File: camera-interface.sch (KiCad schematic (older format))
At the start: 30 parts, among them J8 WE_68715014522, U19 NTS0102GT, U20 NTS0102GT, U22 AP2114H-3_3TRG1

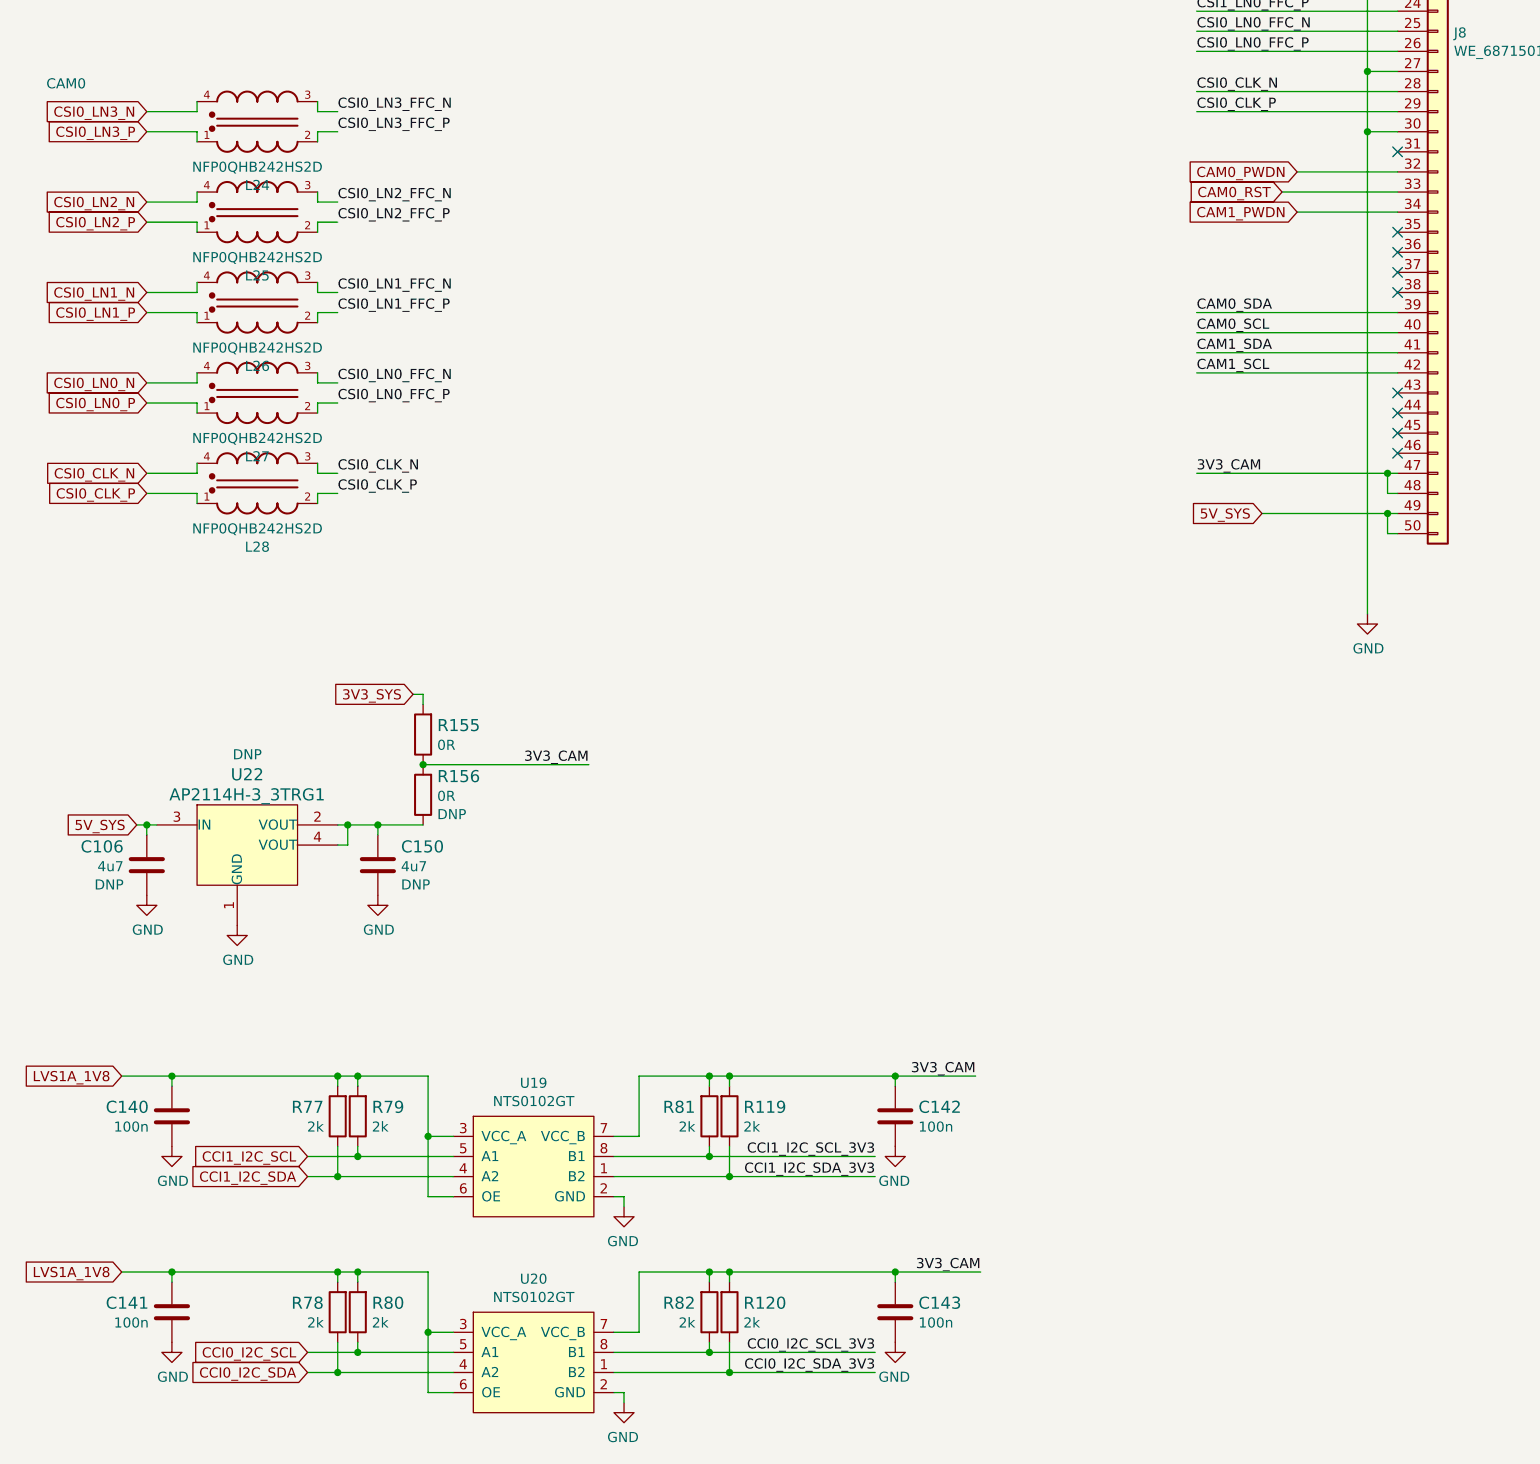
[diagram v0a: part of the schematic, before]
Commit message: Add test points
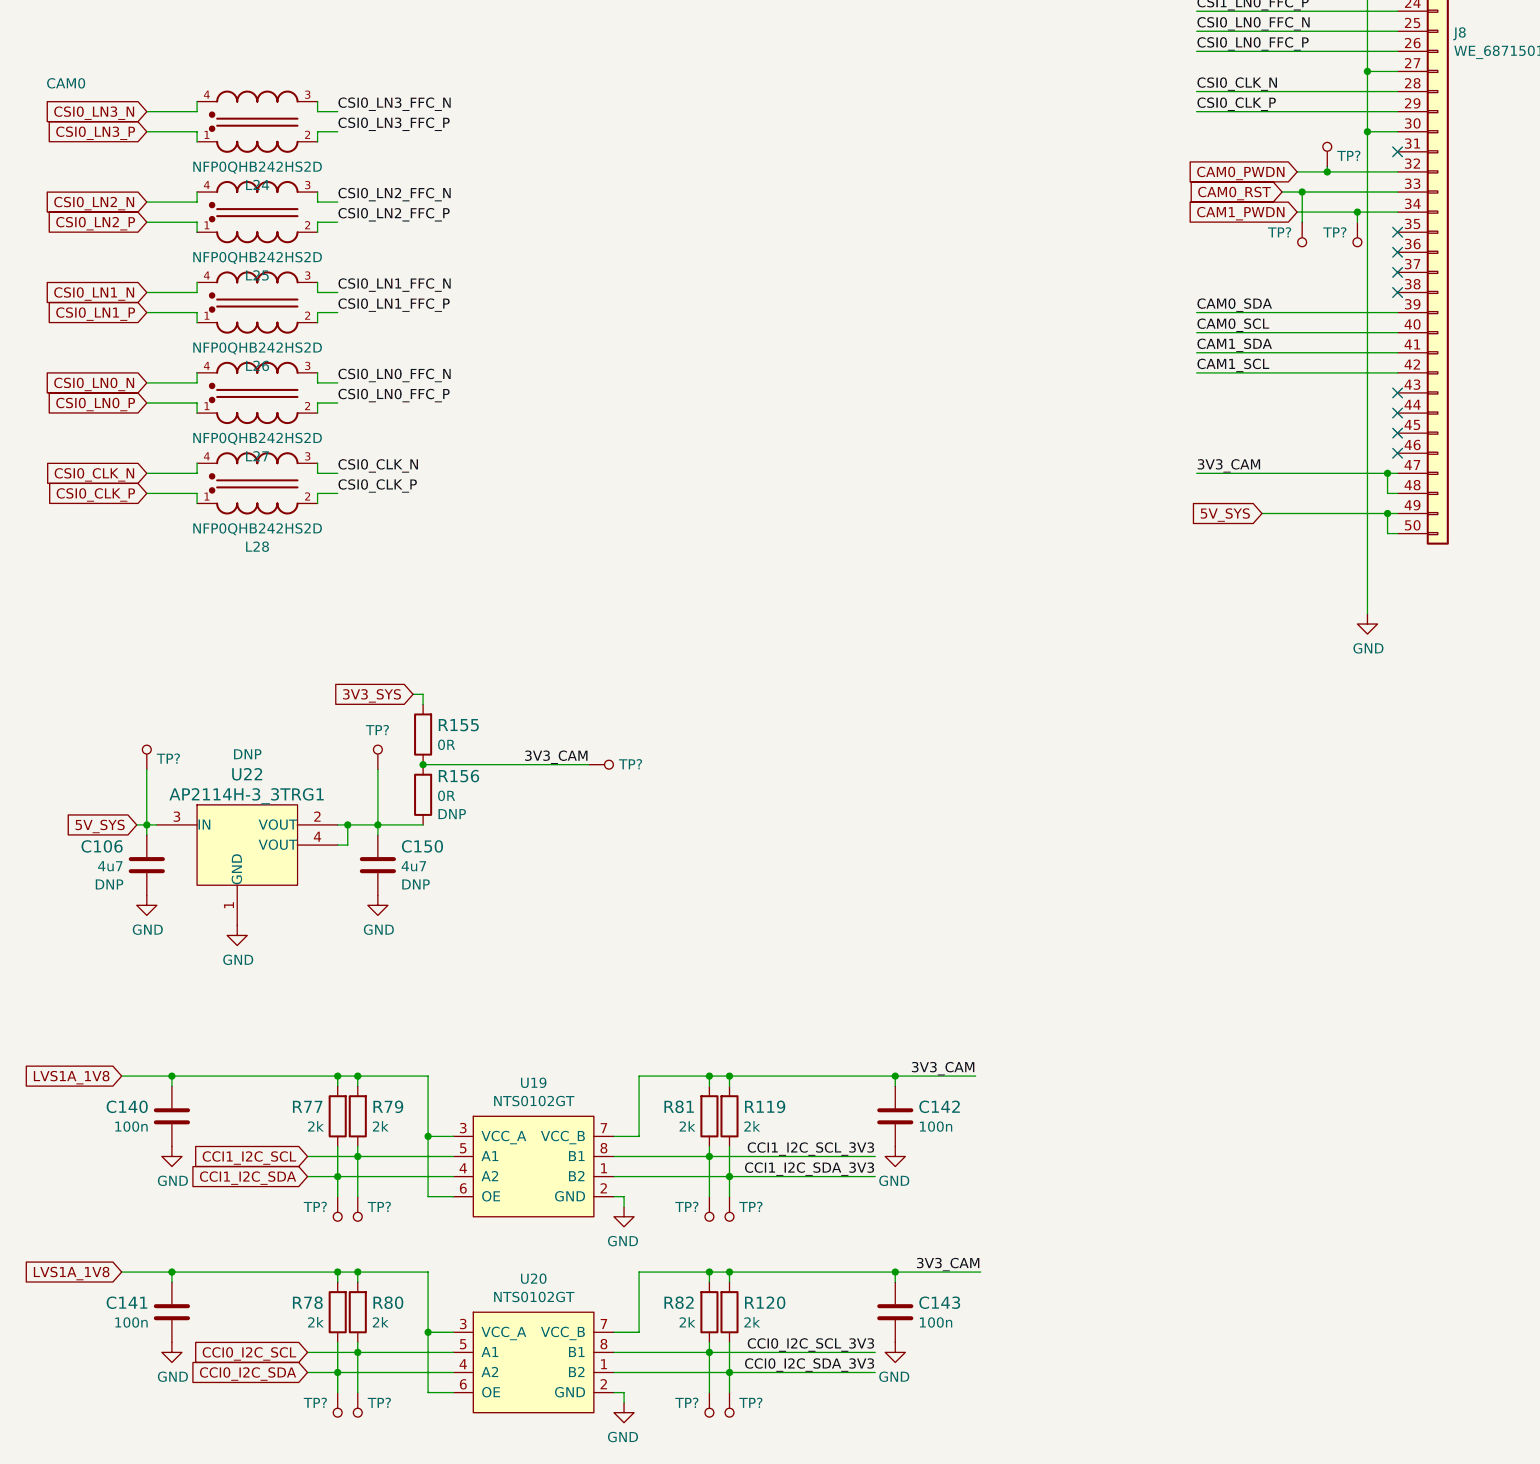
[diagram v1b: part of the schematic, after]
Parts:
- added TP? (x14): TP_SMD_0_75MM, antmicro-footprints:Testpoint_smd_0_75mm, symbol antmicroTestPoints:TP_SMD_0_75MM
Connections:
- net 3V3_CAM: now also TP?.1
- net 5V_SYS: now also TP?.1
- net CAM0_PWDN: now also TP?.1
- net CAM0_RST: now also TP?.1
- net CAM1_PWDN: now also TP?.1
- net CCI0_I2C_SCL: now also TP?.1
- net CCI0_I2C_SCL_3V3: now also TP?.1
- net CCI0_I2C_SDA: now also TP?.1
- net CCI0_I2C_SDA_3V3: now also TP?.1
- net CCI1_I2C_SCL: now also TP?.1
- net CCI1_I2C_SCL_3V3: now also TP?.1
- net CCI1_I2C_SDA: now also TP?.1
- net CCI1_I2C_SDA_3V3: now also TP?.1
- net at C150.1, R156.1, U22.2 (VOUT)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: now also TP?.1
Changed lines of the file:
@@
 NoConn ~ 7450 4650
 Wire Wire Line
-	7450 4750 6950 4750
-Wire Wire Line
-	7450 4850 6875 4850
-Wire Wire Line
-	7450 4950 6950 4950
+	7450 4750 7100 4750
+Wire Wire Line
+	7450 4850 6975 4850
+Wire Wire Line
+	7450 4950 7250 4950
 Text GLabel 6950 4750 0    50   Input ~ 0
 CAM0_PWDN
@@
 	2375 8000 2600 8000
 Connection ~ 2375 8000
-Wire Wire Line
-	1275 8000 1225 8000
-Wire Wire Line
-	1225 8000 1225 8050
 $Comp
 L sa800u-baseboard-hw:GND #PWR0250
@@
 Wire Wire Line
 	7400 6250 7450 6250
+$Comp
+L antmicroTestPoints:TP_SMD_0_75MM TP?
+U 1 1 62E2A94F
+P 4125 9950
+AR Path="/618E716E/62E2A94F" Ref="TP?"  Part="1"
+AR Path="/6197686D/62E2A94F" Ref="TP?"  Part="1"
+F 0 "TP?" H 4076 9997 50  0000 R CNN
+F 1 "TP_SMD_0_75MM" H 4125 9850 50  0001 C CNN
+F 2 "antmicro-footprints:Testpoint_smd_0_75mm" H 4325 10150 60  0001 L CNN
+F 3 "" H 4325 10250 60  0001 L CNN
+	1    4125 9950
+	-1   0    0    -1
+$EndComp
+$Comp
+L antmicroTestPoints:TP_SMD_0_75MM TP?
+U 1 1 62E2A955
+P 4025 9950
+AR Path="/618E716E/62E2A955" Ref="TP?"  Part="1"
+AR Path="/6197686D/62E2A955" Ref="TP?"  Part="1"
+F 0 "TP?" H 4075 9997 50  0000 L CNN
+F 1 "TP_SMD_0_75MM" H 4025 9850 50  0001 C CNN
+F 2 "antmicro-footprints:Testpoint_smd_0_75mm" H 4225 10150 60  0001 L CNN
+F 3 "" H 4225 10250 60  0001 L CNN
+	1    4025 9950
+	-1   0    0    -1
+$EndComp
+Wire Wire Line
+	4125 9850 4125 9750
+Wire Wire Line
+	4025 9850 4025 9650
+$Comp
+L antmicroTestPoints:TP_SMD_0_75MM TP?
+U 1 1 62E363CD
+P 4125 10925
+AR Path="/618E716E/62E363CD" Ref="TP?"  Part="1"
+AR Path="/6197686D/62E363CD" Ref="TP?"  Part="1"
+F 0 "TP?" H 4076 10972 50  0000 R CNN
+F 1 "TP_SMD_0_75MM" H 4125 10825 50  0001 C CNN
+F 2 "antmicro-footprints:Testpoint_smd_0_75mm" H 4325 11125 60  0001 L CNN
+F 3 "" H 4325 11225 60  0001 L CNN
+	1    4125 10925
+	-1   0    0    -1
+$EndComp
+$Comp
+L antmicroTestPoints:TP_SMD_0_75MM TP?
+U 1 1 62E363D3
+P 4025 10925
+AR Path="/618E716E/62E363D3" Ref="TP?"  Part="1"
+AR Path="/6197686D/62E363D3" Ref="TP?"  Part="1"
+F 0 "TP?" H 4075 10972 50  0000 L CNN
+F 1 "TP_SMD_0_75MM" H 4025 10825 50  0001 C CNN
+F 2 "antmicro-footprints:Testpoint_smd_0_75mm" H 4225 11125 60  0001 L CNN
+F 3 "" H 4225 11225 60  0001 L CNN
+	1    4025 10925
+	-1   0    0    -1
+$EndComp
+Wire Wire Line
+	4125 10825 4125 10725
+Wire Wire Line
+	4025 10825 4025 10625
+$Comp
+L antmicroTestPoints:TP_SMD_0_75MM TP?
+U 1 1 62E41C82
+P 2175 10925
+AR Path="/618E716E/62E41C82" Ref="TP?"  Part="1"
+AR Path="/6197686D/62E41C82" Ref="TP?"  Part="1"
+F 0 "TP?" H 2126 10972 50  0000 R CNN
+F 1 "TP_SMD_0_75MM" H 2175 10825 50  0001 C CNN
+F 2 "antmicro-footprints:Testpoint_smd_0_75mm" H 2375 11125 60  0001 L CNN
+F 3 "" H 2375 11225 60  0001 L CNN
+	1    2175 10925
+	1    0    0    -1
+$EndComp
+$Comp
+L antmicroTestPoints:TP_SMD_0_75MM TP?
+U 1 1 62E41C88
+P 2275 10925
+AR Path="/618E716E/62E41C88" Ref="TP?"  Part="1"
+AR Path="/6197686D/62E41C88" Ref="TP?"  Part="1"
+F 0 "TP?" H 2325 10972 50  0000 L CNN
+F 1 "TP_SMD_0_75MM" H 2275 10825 50  0001 C CNN
+F 2 "antmicro-footprints:Testpoint_smd_0_75mm" H 2475 11125 60  0001 L CNN
+F 3 "" H 2475 11225 60  0001 L CNN
+	1    2275 10925
+	1    0    0    -1
+$EndComp
+Wire Wire Line
+	2175 10825 2175 10725
+Wire Wire Line
+	2275 10825 2275 10625
+$Comp
+L antmicroTestPoints:TP_SMD_0_75MM TP?
+U 1 1 62E4DB47
+P 2175 9950
+AR Path="/618E716E/62E4DB47" Ref="TP?"  Part="1"
+AR Path="/6197686D/62E4DB47" Ref="TP?"  Part="1"
+F 0 "TP?" H 2126 9997 50  0000 R CNN
+F 1 "TP_SMD_0_75MM" H 2175 9850 50  0001 C CNN
+F 2 "antmicro-footprints:Testpoint_smd_0_75mm" H 2375 10150 60  0001 L CNN
+F 3 "" H 2375 10250 60  0001 L CNN
+	1    2175 9950
+	1    0    0    -1
+$EndComp
+$Comp
+L antmicroTestPoints:TP_SMD_0_75MM TP?
+U 1 1 62E4DB4D
+P 2275 9950
+AR Path="/618E716E/62E4DB4D" Ref="TP?"  Part="1"
+AR Path="/6197686D/62E4DB4D" Ref="TP?"  Part="1"
+F 0 "TP?" H 2325 9997 50  0000 L CNN
+F 1 "TP_SMD_0_75MM" H 2275 9850 50  0001 C CNN
+F 2 "antmicro-footprints:Testpoint_smd_0_75mm" H 2475 10150 60  0001 L CNN
+F 3 "" H 2475 10250 60  0001 L CNN
+	1    2275 9950
+	1    0    0    -1
+$EndComp
+Wire Wire Line
+	2175 9850 2175 9750
+Wire Wire Line
+	2275 9850 2275 9650
+$Comp
+L antmicroTestPoints:TP_SMD_0_75MM TP?
+U 1 1 62E6257B
+P 1225 7625
+AR Path="/618E716E/62E6257B" Ref="TP?"  Part="1"
+AR Path="/6197686D/62E6257B" Ref="TP?"  Part="1"
+AR Path="/61A60486/62E6257B" Ref="TP?"  Part="1"
+F 0 "TP?" H 1175 7672 50  0000 R CNN
+F 1 "TP_SMD_0_75MM" H 1225 7525 50  0001 C CNN
+F 2 "antmicro-footprints:Testpoint_smd_0_75mm" H 1425 7825 60  0001 L CNN
+F 3 "" H 1425 7925 60  0001 L CNN
+	1    1225 7625
+	-1   0    0    1
+$EndComp
+Wire Wire Line
+	1275 8000 1225 8000
+Wire Wire Line
+	1225 8000 1225 8050
+Wire Wire Line
+	1225 7725 1225 8000
+$Comp
+L antmicroTestPoints:TP_SMD_0_75MM TP?
+U 1 1 62E9438C
+P 2375 7625
+AR Path="/618E716E/62E9438C" Ref="TP?"  Part="1"
+AR Path="/6197686D/62E9438C" Ref="TP?"  Part="1"
+AR Path="/61A60486/62E9438C" Ref="TP?"  Part="1"
+F 0 "TP?" H 2375 7530 50  0000 C CNN
+F 1 "TP_SMD_0_75MM" H 2375 7525 50  0001 C CNN
+F 2 "antmicro-footprints:Testpoint_smd_0_75mm" H 2575 7825 60  0001 L CNN
+F 3 "" H 2575 7925 60  0001 L CNN
+	1    2375 7625
+	-1   0    0    1
+$EndComp
+Wire Wire Line
+	2375 7725 2375 8000
+$Comp
+L antmicroTestPoints:TP_SMD_0_75MM TP?
+U 1 1 62EA24BE
+P 3525 7700
+AR Path="/618E716E/62EA24BE" Ref="TP?"  Part="1"
+AR Path="/6197686D/62EA24BE" Ref="TP?"  Part="1"
+AR Path="/61A60486/62EA24BE" Ref="TP?"  Part="1"
+F 0 "TP?" V 3525 7650 50  0000 R CNN
+F 1 "TP_SMD_0_75MM" H 3525 7600 50  0001 C CNN
+F 2 "antmicro-footprints:Testpoint_smd_0_75mm" H 3725 7900 60  0001 L CNN
+F 3 "" H 3725 8000 60  0001 L CNN
+	1    3525 7700
+	0    -1   -1   0
+$EndComp
+$Comp
+L antmicroTestPoints:TP_SMD_0_75MM TP?
+U 1 1 62EB9E73
+P 7100 4625
+AR Path="/618E716E/62EB9E73" Ref="TP?"  Part="1"
+AR Path="/6197686D/62EB9E73" Ref="TP?"  Part="1"
+AR Path="/61A60486/62EB9E73" Ref="TP?"  Part="1"
+F 0 "TP?" H 7050 4672 50  0000 R CNN
+F 1 "TP_SMD_0_75MM" H 7100 4525 50  0001 C CNN
+F 2 "antmicro-footprints:Testpoint_smd_0_75mm" H 7300 4825 60  0001 L CNN
+F 3 "" H 7300 4925 60  0001 L CNN
+	1    7100 4625
+	-1   0    0    1
+$EndComp
+Wire Wire Line
+	7100 4725 7100 4750
+Connection ~ 7100 4750
+Wire Wire Line
+	7100 4750 6950 4750
+$Comp
+L antmicroTestPoints:TP_SMD_0_75MM TP?
+U 1 1 62EDF1A3
+P 6975 5100
+AR Path="/618E716E/62EDF1A3" Ref="TP?"  Part="1"
+AR Path="/6197686D/62EDF1A3" Ref="TP?"  Part="1"
+AR Path="/61A60486/62EDF1A3" Ref="TP?"  Part="1"
+F 0 "TP?" H 6925 5147 50  0000 R CNN
+F 1 "TP_SMD_0_75MM" H 6975 5000 50  0001 C CNN
+F 2 "antmicro-footprints:Testpoint_smd_0_75mm" H 7175 5300 60  0001 L CNN
+F 3 "" H 7175 5400 60  0001 L CNN
+	1    6975 5100
+	1    0    0    -1
+$EndComp
+Wire Wire Line
+	6975 5000 6975 4850
+Connection ~ 6975 4850
+Wire Wire Line
+	6975 4850 6875 4850
+$Comp
+L antmicroTestPoints:TP_SMD_0_75MM TP?
+U 1 1 62EF7916
+P 7250 5100
+AR Path="/618E716E/62EF7916" Ref="TP?"  Part="1"
+AR Path="/6197686D/62EF7916" Ref="TP?"  Part="1"
+AR Path="/61A60486/62EF7916" Ref="TP?"  Part="1"
+F 0 "TP?" H 7200 5147 50  0000 R CNN
+F 1 "TP_SMD_0_75MM" H 7250 5000 50  0001 C CNN
+F 2 "antmicro-footprints:Testpoint_smd_0_75mm" H 7450 5300 60  0001 L CNN
+F 3 "" H 7450 5400 60  0001 L CNN
+	1    7250 5100
+	1    0    0    -1
+$EndComp
+Wire Wire Line
+	7250 5000 7250 4950
+Connection ~ 7250 4950
+Wire Wire Line
+	7250 4950 6950 4950
 $EndSCHEMATC
